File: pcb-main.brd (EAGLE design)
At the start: 100 x 80 mm, 22 parts, among them U1 BTA-RX-A, U2 RS3-1205S

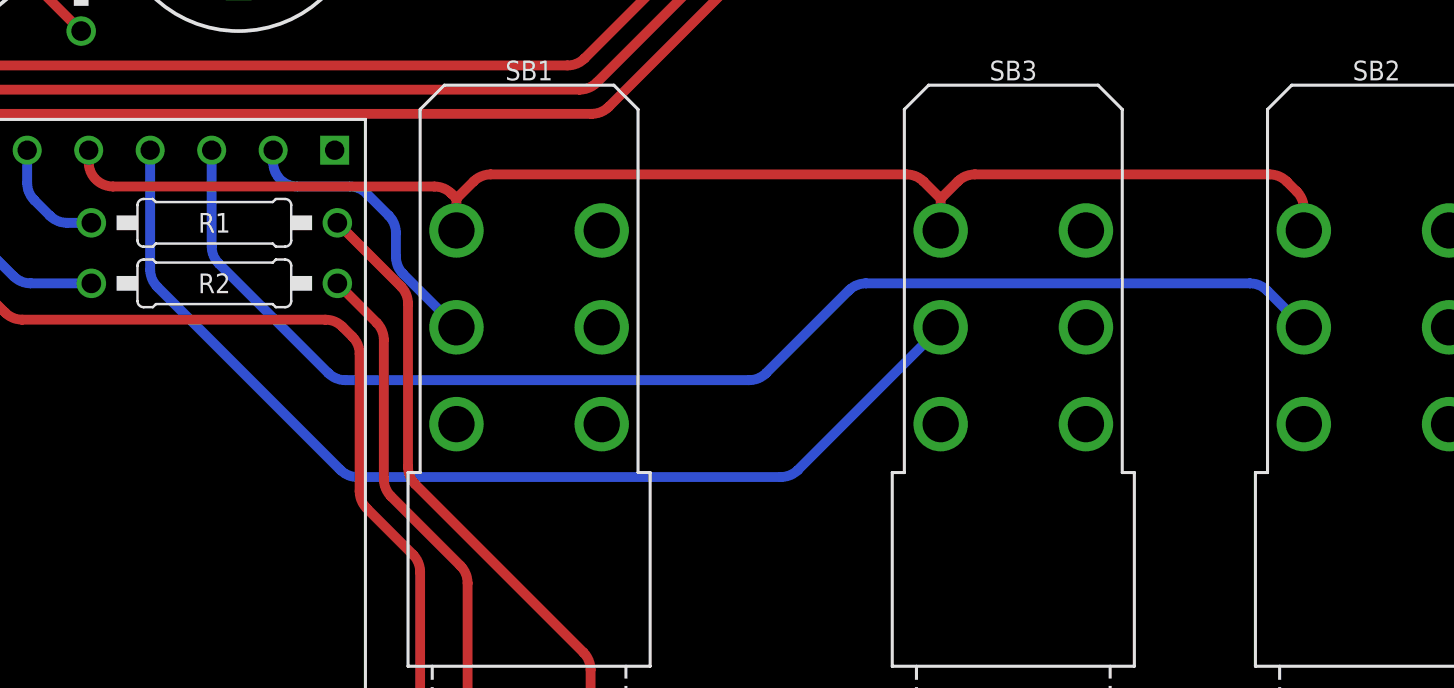
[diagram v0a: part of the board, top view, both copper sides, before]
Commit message: Swap Prev/Next Buttons
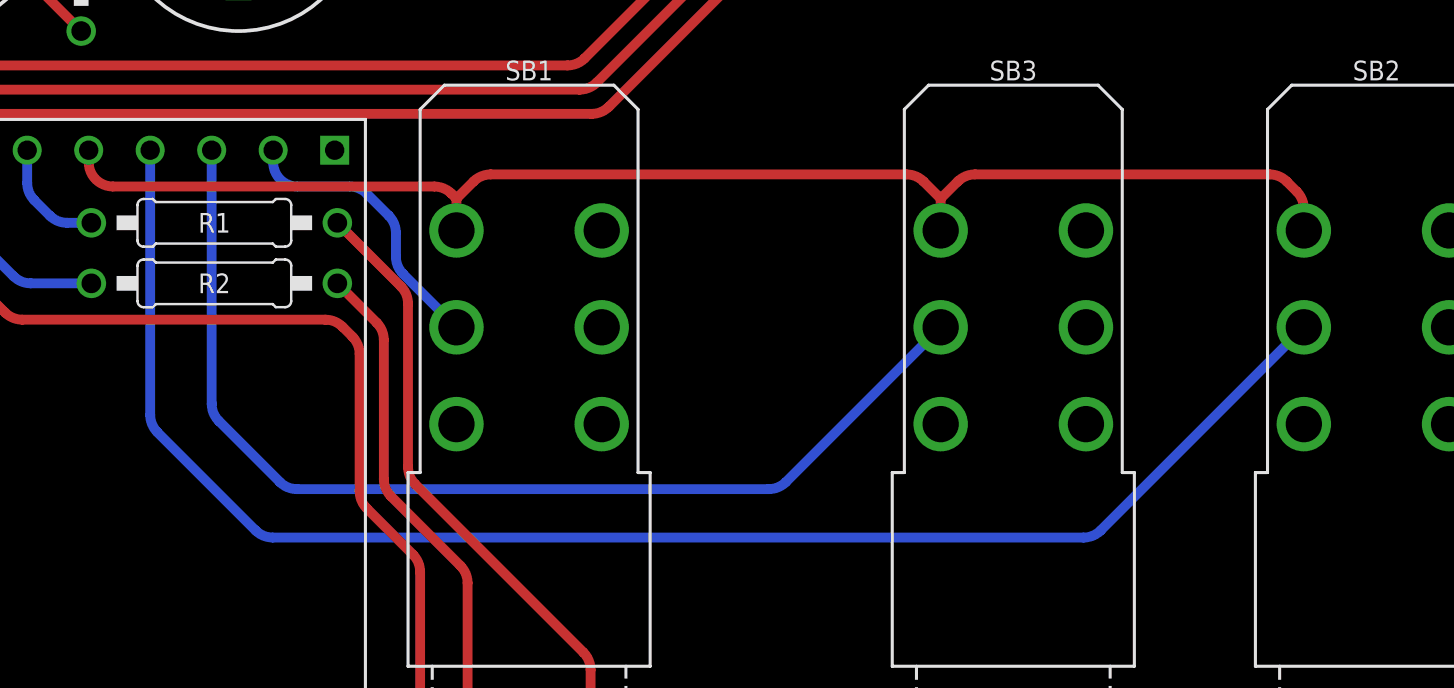
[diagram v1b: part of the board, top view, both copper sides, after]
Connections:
- removed net N$39: SB2.2, U1.3
- removed net N$40: SB3.2, U1.4
- new net N$1: SB2.2, U1.4
- new net N$2: SB3.2, U1.3
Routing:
- net N$1: track 0.00 -> 64.3 mm
- net N$39: track 53.7 -> 0.00 mm
- net N$2: track 0.00 -> 44.9 mm
- net N$40: track 43.7 -> 0.00 mm
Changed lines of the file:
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@@
 <setting verticaltext="up"/>
 </settings>
-<grid distance="0.5" unitdist="mm" unit="mm" style="dots" multiple="1" display="yes" altdistance="0.25" altunitdist="mm" altunit="mm"/>
+<grid distance="1" unitdist="mm" unit="mm" style="dots" multiple="1" display="yes" altdistance="0.25" altunitdist="mm" altunit="mm"/>
 <layers>
 <layer number="1" name="Top" color="4" fill="1" visible="yes" active="yes"/>
@@
 <wire x1="44.79289375" y1="28.89210625" x2="47" y2="26.685" width="0.4064" layer="16"/>
 </signal>
-<signal name="N$39">
-<contactref element="U1" pad="3"/>
-<contactref element="SB2" pad="2"/>
-<wire x1="36.89" y1="34" x2="36.89" y2="30.0242125" width="0.4064" layer="16"/>
-<wire x1="36.89" y1="30.0242125" x2="37.18289375" y2="29.31710625" width="0.4064" layer="16" curve="45"/>
-<wire x1="37.18289375" y1="29.31710625" x2="41.70710625" y2="24.79289375" width="0.4064" layer="16"/>
-<wire x1="41.70710625" y1="24.79289375" x2="42.4142125" y2="24.5" width="0.4064" layer="16" curve="45"/>
-<wire x1="42.4142125" y1="24.5" x2="59.0857875" y2="24.5" width="0.4064" layer="16"/>
-<wire x1="59.0857875" y1="24.5" x2="59.79289375" y2="24.79289375" width="0.4064" layer="16" curve="45"/>
-<wire x1="59.79289375" y1="24.79289375" x2="63.20710625" y2="28.20710625" width="0.4064" layer="16"/>
-<wire x1="63.20710625" y1="28.20710625" x2="63.9142125" y2="28.5" width="0.4064" layer="16" curve="-45"/>
-<wire x1="63.9142125" y1="28.5" x2="79.7707875" y2="28.5" width="0.4064" layer="16"/>
-<wire x1="79.7707875" y1="28.5" x2="80.47789375" y2="28.20710625" width="0.4064" layer="16" curve="-45"/>
-<wire x1="80.47789375" y1="28.20710625" x2="82" y2="26.685" width="0.4064" layer="16"/>
-</signal>
-<signal name="N$40">
-<contactref element="U1" pad="4"/>
-<contactref element="SB3" pad="2"/>
-<wire x1="34.35" y1="34" x2="34.35" y2="29.0642125" width="0.4064" layer="16"/>
-<wire x1="34.35" y1="29.0642125" x2="34.64289375" y2="28.35710625" width="0.4064" layer="16" curve="45"/>
-<wire x1="34.64289375" y1="28.35710625" x2="42.20710625" y2="20.79289375" width="0.4064" layer="16"/>
-<wire x1="42.20710625" y1="20.79289375" x2="42.9142125" y2="20.5" width="0.4064" layer="16" curve="45"/>
-<wire x1="42.9142125" y1="20.5" x2="60.4007875" y2="20.5" width="0.4064" layer="16"/>
-<wire x1="60.4007875" y1="20.5" x2="61.10789375" y2="20.79289375" width="0.4064" layer="16" curve="45"/>
-<wire x1="61.10789375" y1="20.79289375" x2="67" y2="26.685" width="0.4064" layer="16"/>
-</signal>
 <signal name="N$41">
 <contactref element="SB1" pad="3"/>
@@
 <wire x1="37.96" y1="46.5" x2="38" y2="46.54" width="0.4064" layer="16"/>
 </signal>
+<signal name="N$1">
+<contactref element="SB2" pad="2"/>
+<contactref element="U1" pad="4"/>
+<wire x1="34.35" y1="34" x2="34.35" y2="23.0642125" width="0.4064" layer="16"/>
+<wire x1="34.35" y1="23.0642125" x2="34.64289375" y2="22.35710625" width="0.4064" layer="16" curve="45"/>
+<wire x1="34.64289375" y1="22.35710625" x2="38.70710625" y2="18.29289375" width="0.4064" layer="16"/>
+<wire x1="38.70710625" y1="18.29289375" x2="39.4142125" y2="18" width="0.4064" layer="16" curve="45"/>
+<wire x1="39.4142125" y1="18" x2="72.9007875" y2="18" width="0.4064" layer="16"/>
+<wire x1="72.9007875" y1="18" x2="73.60789375" y2="18.29289375" width="0.4064" layer="16" curve="45"/>
+<wire x1="73.60789375" y1="18.29289375" x2="82" y2="26.685" width="0.4064" layer="16"/>
+</signal>
+<signal name="N$2">
+<contactref element="SB3" pad="2"/>
+<contactref element="U1" pad="3"/>
+<wire x1="36.89" y1="34" x2="36.89" y2="23.5242125" width="0.4064" layer="16"/>
+<wire x1="36.89" y1="23.5242125" x2="37.18289375" y2="22.81710625" width="0.4064" layer="16" curve="45"/>
+<wire x1="37.18289375" y1="22.81710625" x2="39.70710625" y2="20.29289375" width="0.4064" layer="16"/>
+<wire x1="39.70710625" y1="20.29289375" x2="40.4142125" y2="20" width="0.4064" layer="16" curve="45"/>
+<wire x1="40.4142125" y1="20" x2="59.9007875" y2="20" width="0.4064" layer="16"/>
+<wire x1="59.9007875" y1="20" x2="60.60789375" y2="20.29289375" width="0.4064" layer="16" curve="45"/>
+<wire x1="60.60789375" y1="20.29289375" x2="67" y2="26.685" width="0.4064" layer="16"/>
+</signal>
 </signals>

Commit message: Bump board revision
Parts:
- PCB1: value IO-BT rev.A -> IO-BT rev.B
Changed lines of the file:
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@@
 <element name="E$1" library="enclosure" package="B*-080" value="" x="0" y="0"/>
 <element name="O1" library="hardware" package="KEYSTONE-7762" value="MOUNT(KEYSTONE-7762)" x="60" y="0"/>
-<element name="PCB1" library="module-footprints" package="F-LOGO" value="IO-BT rev.A" x="48.5" y="78"/>
+<element name="PCB1" library="module-footprints" package="F-LOGO" value="IO-BT rev.B" x="48.5" y="78"/>
 <element name="XS2" library="connectors" package="NMJ6HC-S" value="ACJS-MHR" x="85" y="80" rot="R90">
 <attribute name="MOUSER" value="523-ACJS-MHR" x="85" y="80" size="1.778" layer="27" rot="R90" display="off"/>

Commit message: Increase TRS connector spacing (#1)
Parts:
- moved XS3 2.00 mm to (64.0, 80.0)
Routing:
- net N$35: track 119.4 -> 118.5 mm
- net N$37: track 65.8 -> 65.0 mm
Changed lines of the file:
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@@
 <attribute name="MOUSER" value="523-ACJS-MHR" x="85" y="80" size="1.778" layer="27" rot="R90" display="off"/>
 </element>
-<element name="XS3" library="connectors" package="NMJ6HC-S" value="ACJS-MHR" x="66" y="80" rot="R90">
-<attribute name="MOUSER" value="523-ACJS-MHR" x="66" y="80" size="1.778" layer="27" rot="R90" display="off"/>
+<element name="XS3" library="connectors" package="NMJ6HC-S" value="ACJS-MHR" x="64" y="80" rot="R90">
+<attribute name="MOUSER" value="523-ACJS-MHR" x="64" y="80" size="1.778" layer="27" rot="R90" display="off"/>
 </element>
 <element name="U1" library="module-wireless" package="BTA-RX" value="BTA-RX-A" x="28" y="34" rot="R180"/>
@@
 <contactref element="XS2" pad="R"/>
 <contactref element="XS3" pad="R"/>
-<wire x1="57.885" y1="69.65" x2="57.885" y2="76" width="0.4064" layer="1"/>
+<wire x1="55.885" y1="69.65" x2="55.885" y2="73.115" width="0.4064" layer="1"/>
 <wire x1="76.885" y1="69.65" x2="76.885" y2="73" width="0.4064" layer="1"/>
 <wire x1="76.885" y1="73" x2="76.885" y2="76" width="0.4064" layer="1"/>
-<wire x1="57.885" y1="76" x2="57.885" y2="73.115" width="0.4064" layer="1"/>
-<wire x1="57.885" y1="73.115" x2="58" y2="73" width="0.4064" layer="1"/>
-<wire x1="58" y1="73" x2="66" y2="73" width="0.4064" layer="1"/>
+<wire x1="55.885" y1="76" x2="55.885" y2="73.115" width="0.4064" layer="1"/>
+<wire x1="55.885" y1="73.115" x2="56" y2="73" width="0.4064" layer="1"/>
+<wire x1="56" y1="73" x2="66" y2="73" width="0.4064" layer="1"/>
 <wire x1="66" y1="73" x2="76.885" y2="73" width="0.4064" layer="1"/>
 <wire x1="14.03" y1="34" x2="14.03" y2="33" width="0.4064" layer="1"/>
@@
 <wire x1="18.9142125" y1="37.5" x2="51.5857875" y2="37.5" width="0.4064" layer="1"/>
 <wire x1="51.5857875" y1="37.5" x2="52.29289375" y2="37.79289375" width="0.4064" layer="1" curve="45"/>
-<wire x1="52.29289375" y1="37.79289375" x2="57.25" y2="42.75" width="0.4064" layer="1"/>
-<wire x1="57.25" y1="42.75" x2="57.5" y2="43" width="0.4064" layer="1"/>
-<wire x1="57.885" y1="63.3" x2="57.885" y2="43.7992125" width="0.4064" layer="1"/>
-<wire x1="57.885" y1="43.7992125" x2="57.59210625" y2="43.09210625" width="0.4064" layer="1" curve="-45"/>
-<wire x1="57.59210625" y1="43.09210625" x2="57.5" y2="43" width="0.4064" layer="1"/>
+<wire x1="52.29289375" y1="37.79289375" x2="55.59210625" y2="41.09210625" width="0.4064" layer="1"/>
+<wire x1="55.885" y1="63.3" x2="55.885" y2="41.7992125" width="0.4064" layer="1"/>
+<wire x1="55.885" y1="41.7992125" x2="55.59210625" y2="41.09210625" width="0.4064" layer="1" curve="-45"/>
 </signal>
 <signal name="N$38">

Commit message: Change TRS positioning (#1)
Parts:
- moved XS3 1.00 mm to (65.0, 80.0)
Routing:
- net N$35: track 118.5 -> 117.5 mm
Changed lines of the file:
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@@
 <attribute name="MOUSER" value="523-ACJS-MHR" x="85" y="80" size="1.778" layer="27" rot="R90" display="off"/>
 </element>
-<element name="XS3" library="connectors" package="NMJ6HC-S" value="ACJS-MHR" x="64" y="80" rot="R90">
-<attribute name="MOUSER" value="523-ACJS-MHR" x="64" y="80" size="1.778" layer="27" rot="R90" display="off"/>
+<element name="XS3" library="connectors" package="NMJ6HC-S" value="ACJS-MHR" x="65" y="80" rot="R90">
+<attribute name="MOUSER" value="523-ACJS-MHR" x="65" y="80" size="1.778" layer="27" rot="R90" display="off"/>
 </element>
 <element name="U1" library="module-wireless" package="BTA-RX" value="BTA-RX-A" x="28" y="34" rot="R180"/>
@@
 <contactref element="XS2" pad="R"/>
 <contactref element="XS3" pad="R"/>
-<wire x1="55.885" y1="69.65" x2="55.885" y2="73.115" width="0.4064" layer="1"/>
+<wire x1="56.885" y1="69.65" x2="56.885" y2="73.115" width="0.4064" layer="1"/>
 <wire x1="76.885" y1="69.65" x2="76.885" y2="73" width="0.4064" layer="1"/>
 <wire x1="76.885" y1="73" x2="76.885" y2="76" width="0.4064" layer="1"/>
-<wire x1="55.885" y1="76" x2="55.885" y2="73.115" width="0.4064" layer="1"/>
-<wire x1="55.885" y1="73.115" x2="56" y2="73" width="0.4064" layer="1"/>
-<wire x1="56" y1="73" x2="66" y2="73" width="0.4064" layer="1"/>
+<wire x1="56.885" y1="76" x2="56.885" y2="73.115" width="0.4064" layer="1"/>
+<wire x1="56.885" y1="73.115" x2="57" y2="73" width="0.4064" layer="1"/>
+<wire x1="57" y1="73" x2="66" y2="73" width="0.4064" layer="1"/>
 <wire x1="66" y1="73" x2="76.885" y2="73" width="0.4064" layer="1"/>
 <wire x1="14.03" y1="34" x2="14.03" y2="33" width="0.4064" layer="1"/>
@@
 <wire x1="18.9142125" y1="37.5" x2="51.5857875" y2="37.5" width="0.4064" layer="1"/>
 <wire x1="51.5857875" y1="37.5" x2="52.29289375" y2="37.79289375" width="0.4064" layer="1" curve="45"/>
-<wire x1="52.29289375" y1="37.79289375" x2="55.59210625" y2="41.09210625" width="0.4064" layer="1"/>
-<wire x1="55.885" y1="63.3" x2="55.885" y2="41.7992125" width="0.4064" layer="1"/>
-<wire x1="55.885" y1="41.7992125" x2="55.59210625" y2="41.09210625" width="0.4064" layer="1" curve="-45"/>
+<wire x1="52.29289375" y1="37.79289375" x2="56.59210625" y2="42.09210625" width="0.4064" layer="1"/>
+<wire x1="56.885" y1="63.3" x2="56.885" y2="42.7992125" width="0.4064" layer="1"/>
+<wire x1="56.885" y1="42.7992125" x2="56.59210625" y2="42.09210625" width="0.4064" layer="1" curve="-45"/>
 </signal>
 <signal name="N$38">
